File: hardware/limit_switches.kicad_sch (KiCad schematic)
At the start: 40 parts

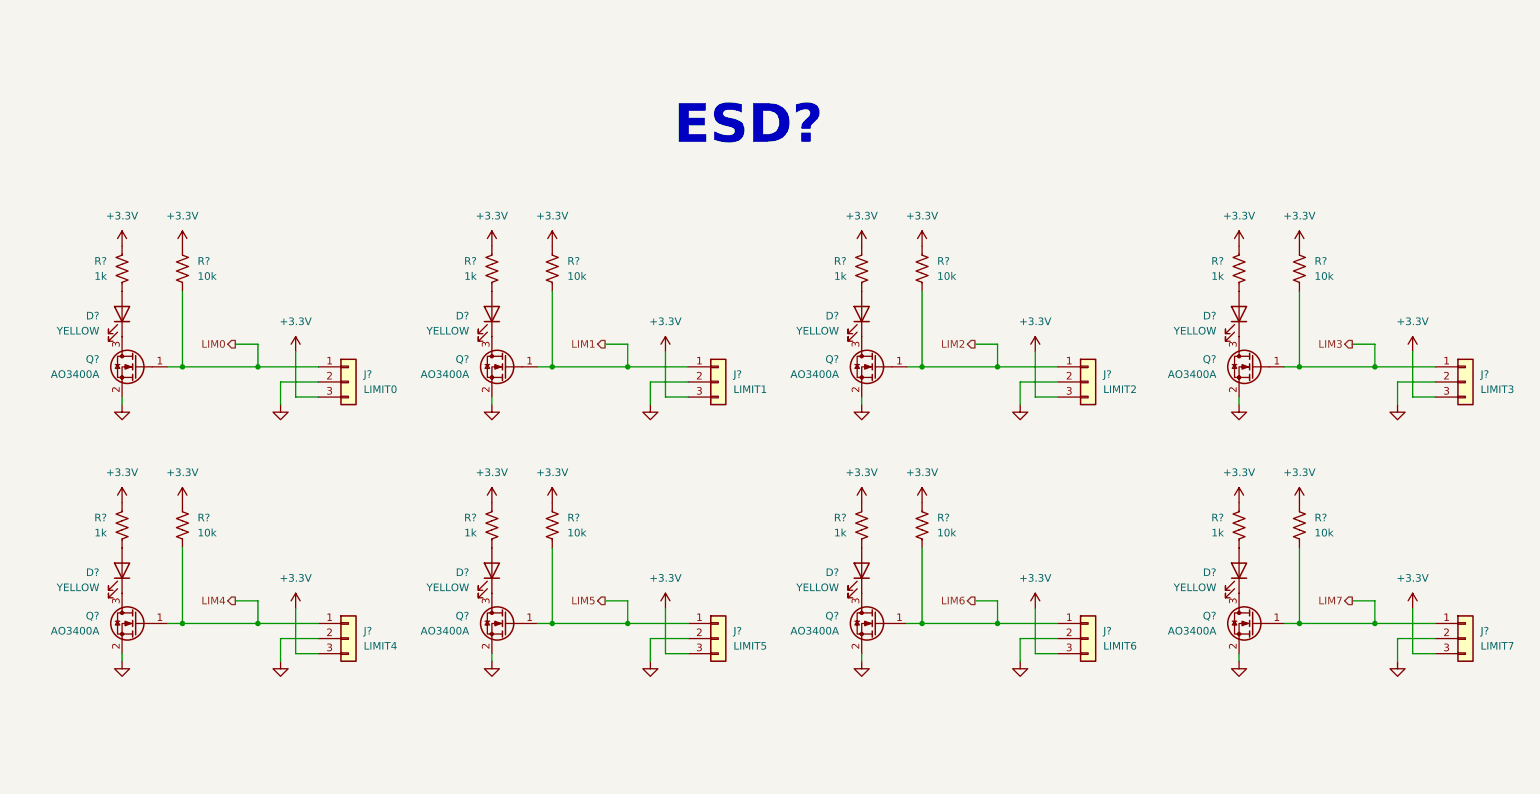
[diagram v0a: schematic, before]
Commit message: Limit Switches and CAN Bus
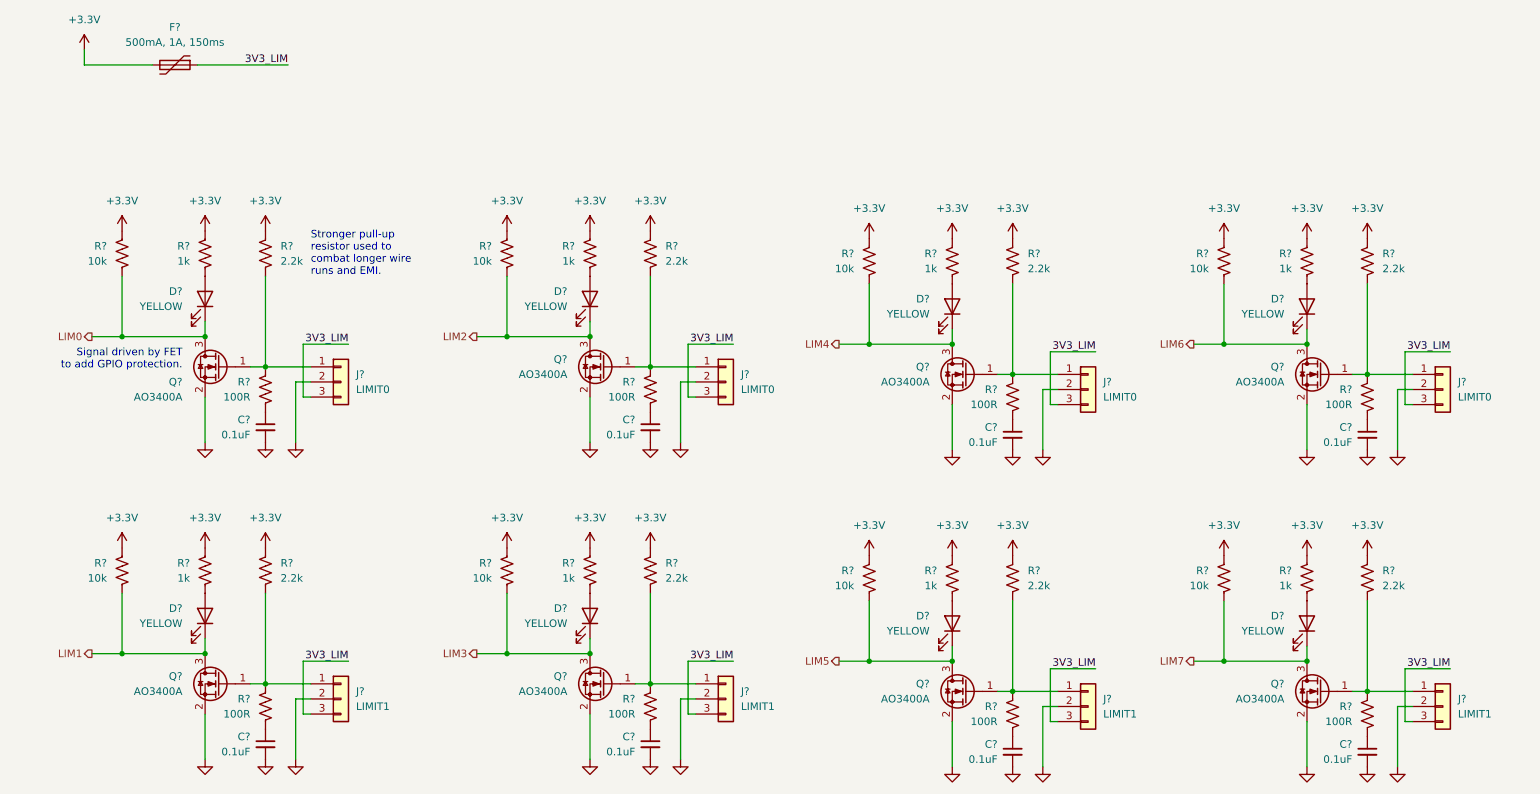
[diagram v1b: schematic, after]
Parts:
- removed D? (x7): YELLOW, Diode_SMD:D_0805_2012Metric, symbol Device:LED
- removed J?: LIMIT6, Connector_JST:JST_XH_S3B-XH-A_1x03_P2.50mm_Horizontal, symbol Connector_Generic:Conn_01x03
- removed J?: LIMIT7, Connector_JST:JST_XH_S3B-XH-A_1x03_P2.50mm_Horizontal, symbol Connector_Generic:Conn_01x03
- removed J?: LIMIT4, Connector_JST:JST_XH_S3B-XH-A_1x03_P2.50mm_Horizontal, symbol Connector_Generic:Conn_01x03
- removed J?: LIMIT3, Connector_JST:JST_XH_S3B-XH-A_1x03_P2.50mm_Horizontal, symbol Connector_Generic:Conn_01x03
- removed J?: LIMIT5, Connector_JST:JST_XH_S3B-XH-A_1x03_P2.50mm_Horizontal, symbol Connector_Generic:Conn_01x03
- removed J?: LIMIT2, Connector_JST:JST_XH_S3B-XH-A_1x03_P2.50mm_Horizontal, symbol Connector_Generic:Conn_01x03
- removed J?: LIMIT1, Connector_JST:JST_XH_S3B-XH-A_1x03_P2.50mm_Horizontal, symbol Connector_Generic:Conn_01x03
- removed Q? (x7): AO3400A, Package_TO_SOT_SMD:SOT-23, symbol Transistor_FET:AO3400A
- removed R? (x7): 1k, Resistor_SMD:R_0603_1608Metric, symbol Device:R_US
- removed R? (x8): 10k, Resistor_SMD:R_0603_1608Metric, symbol Device:R_US
- added C? (x8): 0.1uF, Capacitor_SMD:C_0603_1608Metric_Pad1.08x0.95mm_HandSolder, symbol Device:C_Small
- added D? (x7): YELLOW, Diode_SMD:D_0805_2012Metric, symbol Device:LED
- added F?: 500mA, 1A, 150ms, Fuse:Fuse_1812_4532Metric, symbol Device:Polyfuse
- added J? (x4): LIMIT1, Connector_JST:JST_XH_S3B-XH-A_1x03_P2.50mm_Horizontal, symbol Connector_Generic:Conn_01x03
- added J? (x3): LIMIT0, Connector_JST:JST_XH_S3B-XH-A_1x03_P2.50mm_Horizontal, symbol Connector_Generic:Conn_01x03
- added Q? (x7): AO3400A, Package_TO_SOT_SMD:SOT-23, symbol Transistor_FET:AO3400A
- added R? (x7): 1k, Resistor_SMD:R_0603_1608Metric, symbol Device:R_US
- added R? (x8): 2.2k, Resistor_SMD:R_0603_1608Metric, symbol Device:R_US
- added R? (x8): 100R, Resistor_SMD:R_0603_1608Metric, symbol Device:R_US
- added R? (x8): 10k, Resistor_SMD:R_0603_1608Metric, symbol Device:R_US
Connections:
- net +3.3V: now also F?.2, R?.1, R?.1, R?.1, R?.1, R?.1, R?.1, R?.1, R?.1, R?.1, R?.1, R?.1, R?.1, R?.1, R?.1, R?.1, R?.2, R?.2, R?.2, R?.2, R?.2, R?.2, R?.2, R?.2; no longer J?.3 (Pin_3)
- net GND: now also C?.2, C?.2, C?.2, C?.2, C?.2, C?.2, C?.2, C?.2, J?.2 (Pin_2), J?.2 (Pin_2), J?.2 (Pin_2), J?.2 (Pin_2), J?.2 (Pin_2), J?.2 (Pin_2), J?.2 (Pin_2), Q?.2 (S), Q?.2 (S), Q?.2 (S), Q?.2 (S), Q?.2 (S), Q?.2 (S), Q?.2 (S)
- net LIM0: now also D?.1 (K), Q?.3 (D), R?.2; no longer J?.1 (Pin_1), Q?.1 (G)
- net LIM1: now also D?.1 (K), Q?.3 (D), R?.2
- net LIM2: now also D?.1 (K), Q?.3 (D), R?.2
- net LIM3: now also D?.1 (K), Q?.3 (D), R?.2
- net LIM4: now also D?.1 (K), Q?.3 (D), R?.2
- net LIM5: now also D?.1 (K), Q?.3 (D), R?.2
- net LIM6: now also D?.1 (K), Q?.3 (D), R?.2
- net LIM7: now also D?.1 (K), Q?.3 (D), R?.2
- new net: D?.2 (A), R?.2 (x7)
- new net: J?.1 (Pin_1), Q?.1 (G), R?.1, R?.2 (x8)
- new net: C?.1, R?.1 (x8)
- new net 3V3_LIM: F?.1, J?.3 (Pin_3), J?.3 (Pin_3), J?.3 (Pin_3), J?.3 (Pin_3), J?.3 (Pin_3), J?.3 (Pin_3), J?.3 (Pin_3), J?.3 (Pin_3)
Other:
- note added: "Signal driven by FET to add GPIO protection."
- note added: "Stronger pull-up resistor used to combat longer wire runs and EMI."
- note removed: "ESD?"
- moved on the sheet: D?, J?, Q?, R?
